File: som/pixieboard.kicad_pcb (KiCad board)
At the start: 8 copper layers, 50 x 50 mm, 75 parts, among them J1 Conn_02x20_Counter_Clockwise, J2 Conn_02x20_Counter_Clockwise, J3 Conn_02x20_Counter_Clockwise, J4 Conn_02x20_Counter_Clockwise, J5 Conn_02x20_Counter_Clockwise, J6 Conn_02x20_Counter_Clockwise, SW1 SW_DIP_x03, U1 XC7A200T-3FBG484E, U2 AS4C256M16D3, U3 AS4C256M16D3

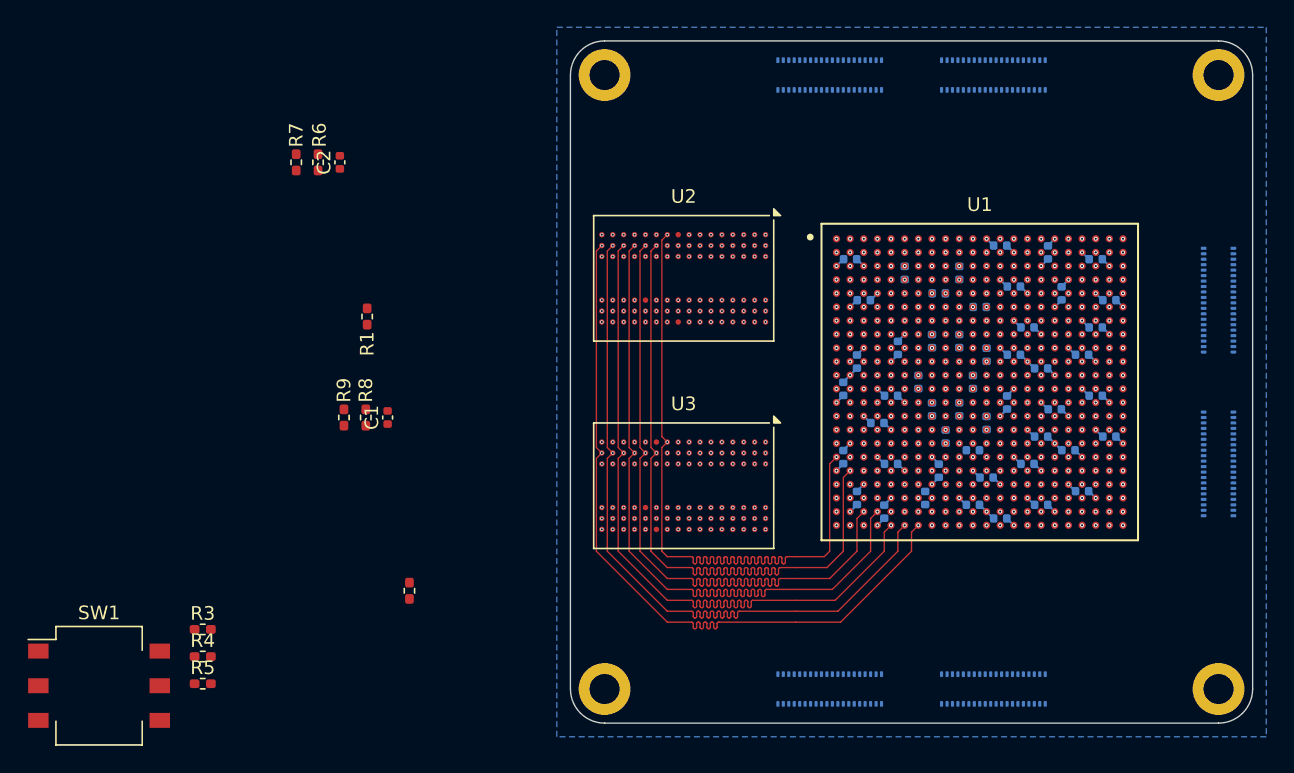
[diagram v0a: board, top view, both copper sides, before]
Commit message: It uses only 3 layers now
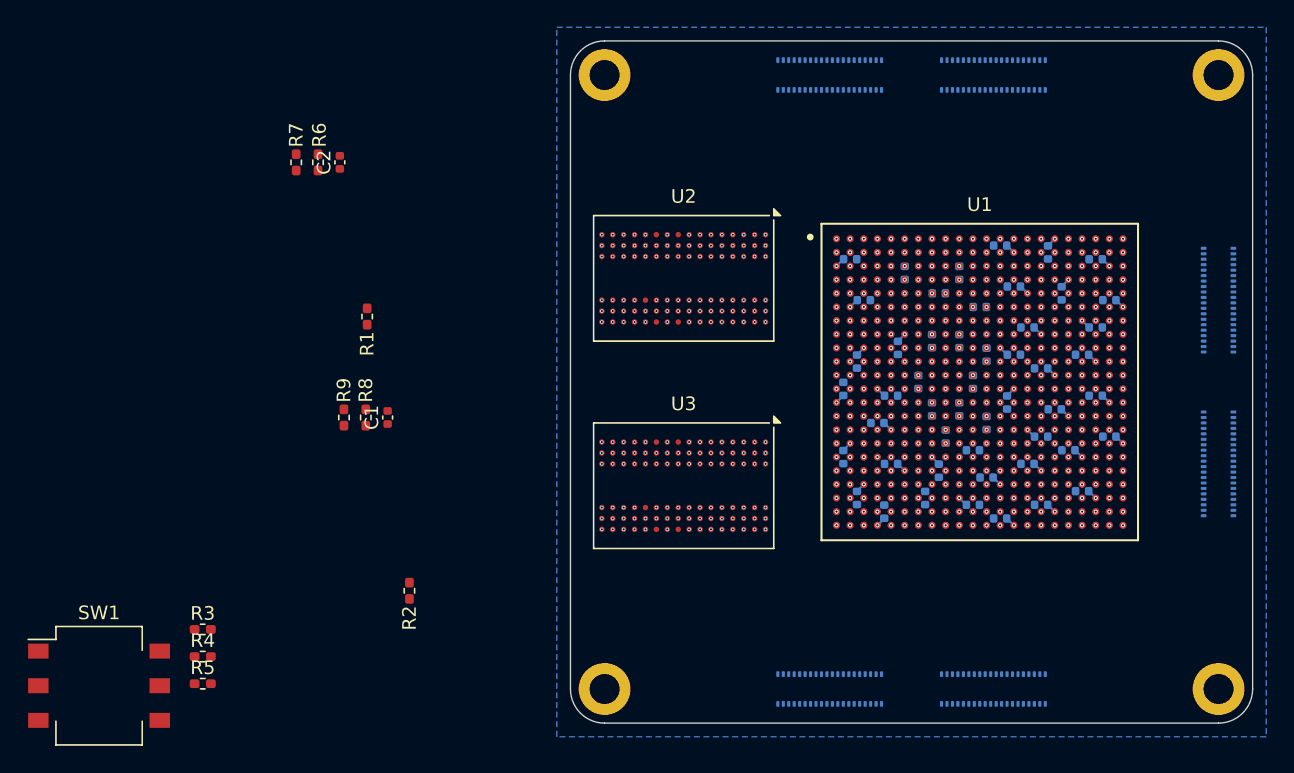
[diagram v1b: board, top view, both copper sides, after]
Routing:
- net /DDR3/~{DDR_RST}: track 55.5 -> 0.00 mm
- net /DDR3/DDR_CLK_E: track 54.4 -> 17.7 mm
- net /DDR3/DDR_A8: track 54.0 -> 18.5 mm
- net /DDR3/DDR_A6: track 54.0 -> 18.5 mm
- net /DDR3/DDR_A4: track 54.0 -> 18.5 mm
- net /DDR3/DDR_A10: track 54.4 -> 19.3 mm
- net /DDR3/DDR_A12: track 54.4 -> 19.3 mm
- net /DDR3/DDR_CLK-: track 54.4 -> 19.3 mm
- net /DDR3/DDR_CLK+: track 54.4 -> 19.3 mm
- net /DDR3/DDR_A14: track 54.5 -> 20.1 mm
- net /DDR3/DDR_A11: track 54.5 -> 20.1 mm
- net /DDR3/DDR_A1: track 54.5 -> 20.1 mm
- net /DDR3/DDR_BA1: track 52.5 -> 18.5 mm
- net /DDR3/DDR_A13: track 55.0 -> 22.9 mm
- net /DDR3/DDR_A9: track 55.0 -> 22.9 mm
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
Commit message: ok
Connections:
- U1 pad AA3: /DDR3/DDR_BA0 -> unconnected-(U1E-IO_L9N_T1_DQS_34-PadAA3)
- U1 pad AA4: /DDR3/DDR_A3 -> unconnected-(U1E-IO_L11N_T1_SRCC_34-PadAA4)
- U1 pad AA5: /DDR3/DDR_A0 -> unconnected-(U1E-IO_L10P_T1_34-PadAA5)
- U1 pad AA6: /DDR3/DDR_A2 -> /DDR3/DDR_A6
- U1 pad AB5: /DDR3/DDR_A5 -> unconnected-(U1E-IO_L10N_T1_34-PadAB5)
- U1 pad AB6: /DDR3/DDR_A7 -> unconnected-(U1E-IO_L20N_T3_34-PadAB6)
- U1 pad AB7: /DDR3/~{DDR_RST} -> /DDR3/DDR_A8
- U1 pad AB8: /DDR3/DDR_A13 -> unconnected-(U1E-IO_L22N_T3_34-PadAB8)
- U1 pad R2: /DDR3/DDR_CLK- -> unconnected-(U1E-IO_L3N_T0_DQS_34-PadR2)
- U1 pad R3: /DDR3/DDR_CLK+ -> unconnected-(U1E-IO_L3P_T0_DQS_34-PadR3)
- U1 pad R6: /DDR3/DDR_CLK_E -> unconnected-(U1E-IO_L17P_T2_34-PadR6)
- U1 pad T1: /DDR3/~{DDR_RAS} -> /DDR3/DDR_CLK+
- U1 pad T4: /DDR3/DDR_A4 -> unconnected-(U1E-IO_L13N_T2_MRCC_34-PadT4)
- U1 pad T6: /DDR3/DDR_A10 -> unconnected-(U1E-IO_L17N_T2_34-PadT6)
- U1 pad U1: /DDR3/DDR_ODT -> /DDR3/DDR_CLK-
- U1 pad U2: /DDR3/~{DDR_CAS} -> /DDR3/DDR_CLK_E
- U1 pad U3: unconnected-(U1E-IO_L6P_T0_34-PadU3) -> /DDR3/DDR_A10
- U1 pad U5: /DDR3/DDR_A6 -> unconnected-(U1E-IO_L14N_T2_SRCC_34-PadU5)
- U1 pad U6: /DDR3/DDR_A8 -> unconnected-(U1E-IO_L16P_T2_34-PadU6)
- U1 pad V2: /DDR3/~{DDR_CS} -> unconnected-(U1E-IO_L2N_T0_34-PadV2)
- U1 pad V5: /DDR3/DDR_A1 -> unconnected-(U1E-IO_L16N_T2_34-PadV5)
- U1 pad W2: /DDR3/DDR_BA1 -> unconnected-(U1E-IO_L4P_T0_34-PadW2)
- U1 pad W5: unconnected-(U1E-IO_L15N_T2_DQS_34-PadW5) -> /DDR3/DDR_BA1
- U1 pad W6: /DDR3/DDR_A11 -> unconnected-(U1E-IO_L15P_T2_DQS_34-PadW6)
- U1 pad W7: /DDR3/DDR_A14 -> unconnected-(U1E-IO_L19N_T3_VREF_34-PadW7)
- U1 pad Y3: /DDR3/~{DDR_WE} -> unconnected-(U1E-IO_L9P_T1_DQS_34-PadY3)
- U1 pad Y4: /DDR3/DDR_BA2 -> unconnected-(U1E-IO_L11P_T1_SRCC_34-PadY4)
- U1 pad Y6: unconnected-(U1E-IO_L18P_T2_34-PadY6) -> /DDR3/DDR_A4
- U1 pad Y7: /DDR3/DDR_A9 -> unconnected-(U1E-IO_L23N_T3_34-PadY7)
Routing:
- net /DDR3/DDR_CLK-: track 19.3 -> 39.1 mm
- net /DDR3/DDR_CLK+: track 19.3 -> 38.5 mm
- net unconnected-(U1E-IO_L9P_T1_DQS_34-PadY3): vias 0 -> 1
- net unconnected-(U1E-IO_L9N_T1_DQS_34-PadAA3): vias 0 -> 1
- net unconnected-(U1E-IO_L6P_T0_34-PadU3): vias 1 -> 0
- net unconnected-(U1E-IO_L4P_T0_34-PadW2): vias 0 -> 1
- net unconnected-(U1E-IO_L3P_T0_DQS_34-PadR3): vias 0 -> 1
- net unconnected-(U1E-IO_L3N_T0_DQS_34-PadR2): vias 0 -> 1
- net unconnected-(U1E-IO_L2N_T0_34-PadV2): vias 0 -> 1
- net unconnected-(U1E-IO_L23N_T3_34-PadY7): vias 0 -> 1
- net unconnected-(U1E-IO_L22N_T3_34-PadAB8): vias 0 -> 1
- net unconnected-(U1E-IO_L20N_T3_34-PadAB6): vias 0 -> 1
- net unconnected-(U1E-IO_L19N_T3_VREF_34-PadW7): vias 0 -> 1
- net unconnected-(U1E-IO_L18P_T2_34-PadY6): vias 1 -> 0
- net unconnected-(U1E-IO_L17P_T2_34-PadR6): vias 0 -> 1
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
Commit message: DDR3 (again)
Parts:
- added C53: 1nF, Capacitor_SMD:C_0402_1005Metric, B.Cu at (-6.00, -7.00)
- added C54: 1nF, Capacitor_SMD:C_0402_1005Metric, B.Cu at (-6.50, 2.50)
- added C55: 1nF, Capacitor_SMD:C_0402_1005Metric, B.Cu at (-3.00, 8.00)
- added C56: 1nF, Capacitor_SMD:C_0402_1005Metric, B.Cu at (-5.50, 5.50)
- moved C16 2.00 mm to (-3.00, 3.00), turned to 0 degrees
- moved C14 1.00 mm to (-6.00, -5.00)
- moved C15 0.71 mm to (-3.50, 5.50), turned to 90 degrees
- moved C51 0.71 mm to (-1.00, 9.00), turned to 0 degrees
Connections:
- C1 pad 1: Net-(U3-VREFCA) -> /DDR_VREF
- C2 pad 1: Net-(U2-VREFCA) -> /DDR_VREF
- U1 pad AA4: unconnected-(U1E-IO_L11N_T1_SRCC_34-PadAA4) -> /DDR3/DDR_A7
- U1 pad AA5: unconnected-(U1E-IO_L10P_T1_34-PadAA5) -> /DDR3/DDR_A2
- U1 pad AA6: /DDR3/DDR_A6 -> unconnected-(U1E-IO_L18N_T2_34-PadAA6)
- U1 pad AA8: unconnected-(U1E-IO_L22P_T3_34-PadAA8) -> /DDR3/DDR_A8
- U1 pad AB5: unconnected-(U1E-IO_L10N_T1_34-PadAB5) -> /DDR3/DDR_A9
- U1 pad AB6: unconnected-(U1E-IO_L20N_T3_34-PadAB6) -> /DDR3/DDR_A13
- U1 pad AB7: /DDR3/DDR_A8 -> /DDR3/DDR_A14
- U1 pad B1: /DDR3/DDR_D6 -> /DDR3/DDR_D2
- U1 pad B2: /DDR3/DDR_D2 -> /DDR3/DDR_D6
- U1 pad E2: /DDR3/DDR_D5 -> /DDR3/DDR_DM0
- U1 pad E3: unconnected-(U1F-IO_L6N_T0_VREF_35-PadE3) -> /DDR_VREF
- U1 pad F1: /DDR3/DDR_D3 -> /DDR3/DDR_D5
- U1 pad F3: /DDR3/DDR_D1 -> /DDR3/DDR_D3
- U1 pad G1: /DDR3/DDR_DM0 -> /DDR3/DDR_D1
- U1 pad G2: /DDR3/DDR_D8 -> /DDR3/DDR_DM1
- U1 pad G3: /DDR3/DDR_D13 -> /DDR3/DDR_D11
- U1 pad G4: unconnected-(U1F-IO_L12N_T1_MRCC_35-PadG4) -> /DDR3/DDR_D15
- U1 pad H2: /DDR3/DDR_D10 -> /DDR3/DDR_D14
- U1 pad H3: /DDR3/DDR_D15 -> /DDR3/DDR_D9
- U1 pad H4: /DDR3/DDR_D11 -> /DDR3/DDR_D12
- U1 pad H5: /DDR3/DDR_DM1 -> /DDR3/DDR_D13
- U1 pad J1: /DDR3/DDR_D12 -> /DDR3/DDR_D8
- U1 pad J4: /DDR3/DDR_D22 -> /DDR3/DDR_D20
- U1 pad J5: /DDR3/DDR_D9 -> unconnected-(U1F-IO_L10P_T1_AD15P_35-PadJ5)
- U1 pad K1: /DDR3/DDR_D14 -> /DDR3/DDR_D10
- U1 pad K3: /DDR3/DDR_D20 -> /DDR3/DDR_D22
- U1 pad K4: unconnected-(U1F-IO_L13P_T2_MRCC_35-PadK4) -> /DDR3/DDR_D23
- U1 pad K6: /DDR3/DDR_D18 -> /DDR3/DDR_DM2
- U1 pad L3: /DDR3/DDR_D21 -> /DDR3/DDR_D18
- U1 pad L6: /DDR3/DDR_D16 -> unconnected-(U1F-IO_25_35-PadL6)
- U1 pad M2: /DDR3/DDR_DM2 -> /DDR3/DDR_D16
- U1 pad M3: /DDR3/DDR_D23 -> /DDR3/DDR_D21
- U1 pad M5: unconnected-(U1F-IO_L23N_T3_35-PadM5) -> /DDR3/DDR_DM3
- U1 pad M6: /DDR3/DDR_D25 -> /DDR3/DDR_D28
- U1 pad N2: /DDR3/DDR_D24 -> /DDR3/DDR_D25
- U1 pad N3: /DDR3/DDR_D29 -> /DDR_VREF
- U1 pad N4: /DDR3/DDR_D31 -> /DDR3/DDR_D27
- U1 pad N5: /DDR3/DDR_D27 -> /DDR3/DDR_D31
- U1 pad P1: /DDR3/DDR_D28 -> /DDR3/DDR_D29
- U1 pad P2: /DDR3/DDR_D26 -> /DDR3/DDR_D24
- U1 pad P6: /DDR3/DDR_DM3 -> /DDR3/DDR_D30
- U1 pad R1: /DDR3/DDR_D30 -> /DDR3/DDR_D26
- U1 pad R3: unconnected-(U1E-IO_L3P_T0_DQS_34-PadR3) -> /DDR3/DDR_CLK_E
- U1 pad R6: unconnected-(U1E-IO_L17P_T2_34-PadR6) -> /DDR3/DDR_A10
- U1 pad T6: unconnected-(U1E-IO_L17N_T2_34-PadT6) -> /DDR3/DDR_A12
- U1 pad U2: /DDR3/DDR_CLK_E -> /DDR3/~{DDR_RAS}
- U1 pad U3: /DDR3/DDR_A10 -> /DDR3/~{DDR_CAS}
- U1 pad U6: unconnected-(U1E-IO_L16P_T2_34-PadU6) -> /DDR3/DDR_BA1
- U1 pad V2: unconnected-(U1E-IO_L2N_T0_34-PadV2) -> /DDR3/~{DDR_WE}
- U1 pad V3: unconnected-(U1E-IO_L6N_T0_VREF_34-PadV3) -> /DDR_VREF
- U1 pad V4: /DDR3/DDR_A12 -> /DDR3/DDR_BA2
- U1 pad V7: unconnected-(U1E-IO_L19P_T3_34-PadV7) -> /DDR3/DDR_A4
- U1 pad W1: unconnected-(U1E-IO_L5P_T0_34-PadW1) -> /DDR3/DDR_ODT
- U1 pad W2: unconnected-(U1E-IO_L4P_T0_34-PadW2) -> /DDR3/~{DDR_CS}
- U1 pad W4: unconnected-(U1E-IO_L12N_T1_MRCC_34-PadW4) -> /DDR3/DDR_A1
- U1 pad W5: /DDR3/DDR_BA1 -> /DDR3/DDR_A0
- U1 pad W7: unconnected-(U1E-IO_L19N_T3_VREF_34-PadW7) -> /DDR_VREF
- U1 pad Y2: unconnected-(U1E-IO_L4N_T0_34-PadY2) -> /DDR3/DDR_BA0
- U1 pad Y3: unconnected-(U1E-IO_L9P_T1_DQS_34-PadY3) -> /DDR3/DDR_A3
- U1 pad Y4: unconnected-(U1E-IO_L11P_T1_SRCC_34-PadY4) -> /DDR3/DDR_A5
- U1 pad Y6: /DDR3/DDR_A4 -> /DDR3/DDR_A11
- U1 pad Y7: unconnected-(U1E-IO_L23N_T3_34-PadY7) -> /DDR3/DDR_A6
- U2 pad H1: Net-(U2-VREFCA) -> /DDR_VREF
- U2 pad M8: Net-(U2-VREFCA) -> /DDR_VREF
- U3 pad H1: Net-(U3-VREFCA) -> /DDR_VREF
- U3 pad M8: Net-(U3-VREFCA) -> /DDR_VREF
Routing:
- net /DDR3/DDR_CLK_E: track 17.7 -> 53.9 mm
- net /DDR3/DDR_A4: track 18.5 -> 54.5 mm
- net /DDR3/DDR_A8: track 18.5 -> 54.0 mm
- net /DDR3/DDR_A6: track 18.5 -> 54.0 mm
- net /DDR3/DDR_BA1: track 18.5 -> 54.0 mm
- net /DDR3/DDR_A12: track 19.3 -> 54.0 mm
- net /DDR3/DDR_A10: track 19.3 -> 54.0 mm
- net /DDR3/DDR_A2: track 22.9 -> 53.0 mm, vias 2 -> 3
- net /DDR3/DDR_A14: track 20.1 -> 50.2 mm, vias 2 -> 3
- net /DDR3/DDR_A11: track 20.1 -> 50.2 mm, vias 2 -> 3
- net /DDR3/~{DDR_WE}: track 22.9 -> 53.0 mm, vias 2 -> 3
- net /DDR3/DDR_A1: track 20.1 -> 50.1 mm, vias 2 -> 3
- net /DDR3/DDR_A5: track 23.7 -> 53.0 mm, vias 2 -> 3
- net /DDR3/DDR_A13: track 22.9 -> 52.2 mm, vias 2 -> 3
- net /DDR3/DDR_A9: track 22.9 -> 52.1 mm, vias 2 -> 3
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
